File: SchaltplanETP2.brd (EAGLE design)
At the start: 110 x 60 mm, 62 parts, among them IC1 LM2674, IC2 ZXLD1350, IC3 ZXLD1350, IC4 ZXLD1350, IC5 ZXLD1350, M1 RN42_BLUETOOTH, T1 BUK98150-55A, X1 TERMINAL_BLOCK_MC000036, X2 TERMINAL_BLOCK_MC000036

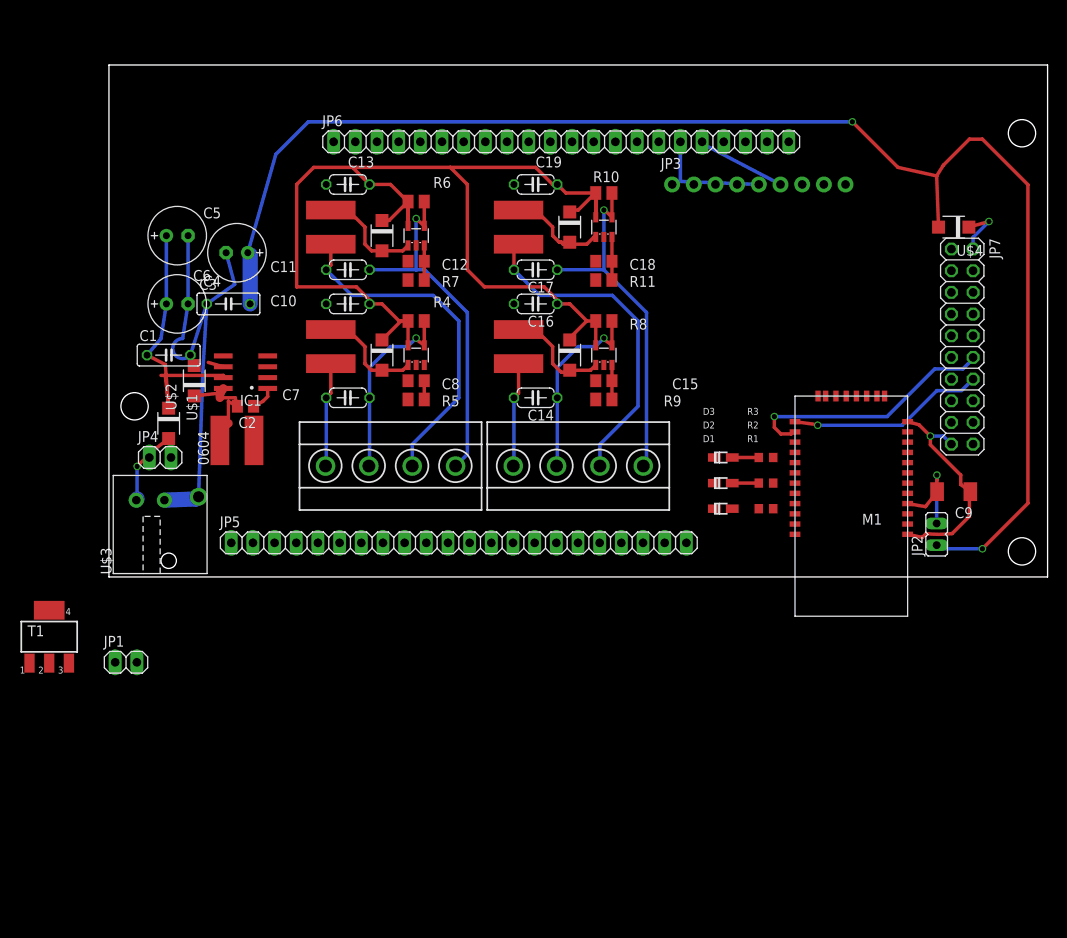
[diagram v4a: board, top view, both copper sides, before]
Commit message: added placed screw terminal and diode for motor driver
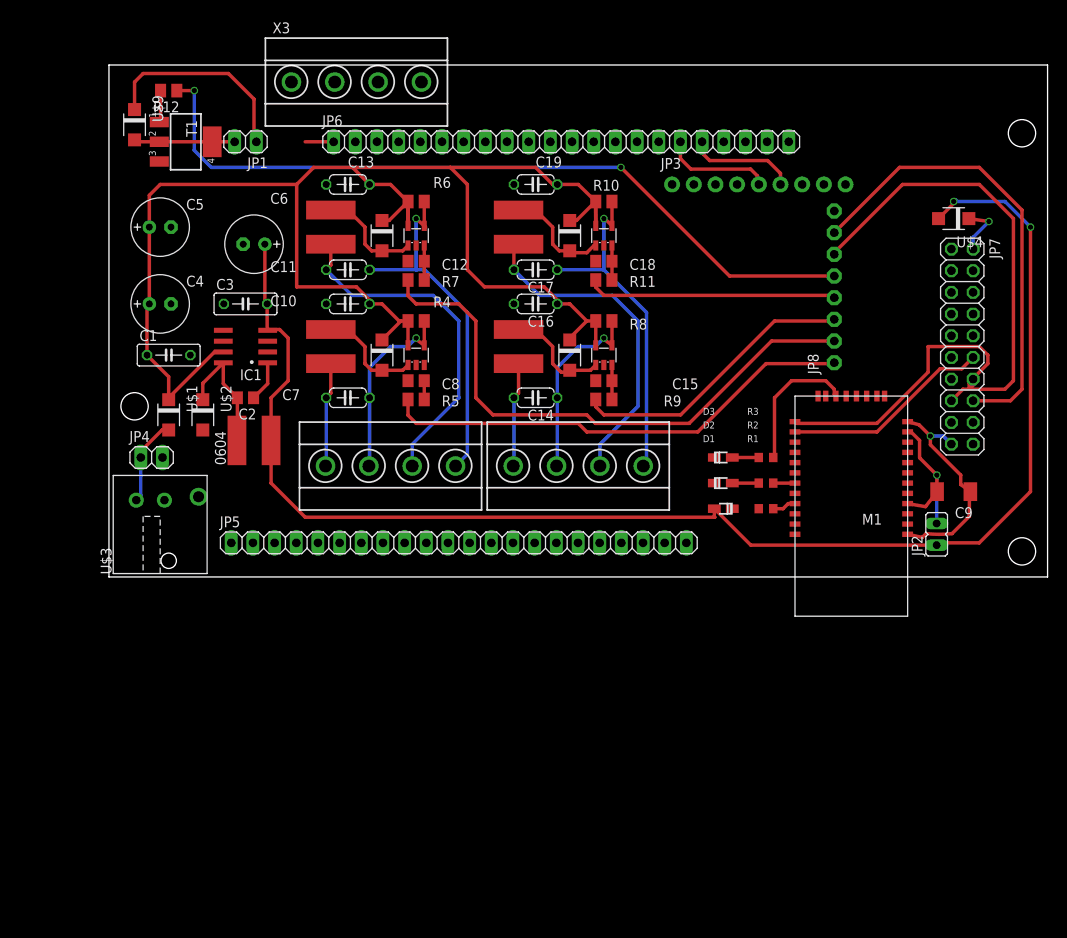
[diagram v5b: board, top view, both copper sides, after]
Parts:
- added JP8: (no value), adafruit:1X08-CLEANBIG
- added R12: 220, rcl:M0805
- added U$9: SS13L, Moodlight:SUB-SMA
- added X3: TERMINAL_BLOCK_MC000036, Moodlight:TERMINAL_BLOCK_MC000036
- moved JP1 62.6 mm to (16.0, 51.0), turned to 180 degrees
- moved T1 60.2 mm to (9.00, 51.0), turned to 270 degrees
- moved U$2 4.12 mm to (11.0, 19.0), turned to 270 degrees
- moved IC1 3.00 mm to (16.0, 27.0)
- moved C5 2.24 mm to (6.00, 41.0)
- moved C6 2.24 mm to (17.0, 39.0)
- moved 0604 2.00 mm to (17.0, 16.0)
- moved C3 2.00 mm to (16.0, 32.0)
- moved C4 2.00 mm to (6.00, 32.0)
- moved C2 1.00 mm to (16.0, 21.0)
- moved IC4 1.00 mm to (58.0, 40.0)
- moved JP4 1.00 mm to (5.00, 14.0)
- moved R10 1.00 mm to (58.0, 44.0)
- moved U$1 1.00 mm to (7.00, 19.0)
- moved U$4 1.00 mm to (99.0, 42.0)
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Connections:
- new net MCU_I2C: JP7.15, JP8.6
- new net MCU_I2C2: JP7.16, JP8.7
- new net M_PWM: JP8.5, R12.1, X3.1
- new net N$1: R12.2, T1.1
- new net N$28: JP8.8
- net 0_PWM: now also JP8.1
- net 1_PWM: now also JP8.2
- net 2_PWM: now also JP8.3
- net 3V3: now also U$9.C
- net 3_PWM: now also JP8.4
- net M-: now also U$9.A, X3.2
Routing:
- net M_PWM: track 0.00 -> 90.2 mm, vias 0 -> 2
- net 1_PWM: track 0.00 -> 67.3 mm
- net GND: track 82.8 -> 25.9 mm
- net 0_PWM: track 0.00 -> 56.0 mm
- net MCU_I2C2: track 0.00 -> 54.5 mm
- net MCU_I2C: track 0.00 -> 53.4 mm
- net 2_PWM: track 0.00 -> 33.8 mm
- net 3_PWM: track 0.00 -> 29.3 mm
- net 3V3: track 0.00 -> 24.0 mm
- net +24V: track 167.9 -> 186.2 mm
- net N$12: track 0.00 -> 16.3 mm
- net M-: track 0.00 -> 12.0 mm
- net RN42_TX: track 23.2 -> 34.9 mm, vias 1 -> 0
- net N$5: track 12.5 -> 19.2 mm
- net RN42_RX: track 30.3 -> 24.5 mm, vias 1 -> 0
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
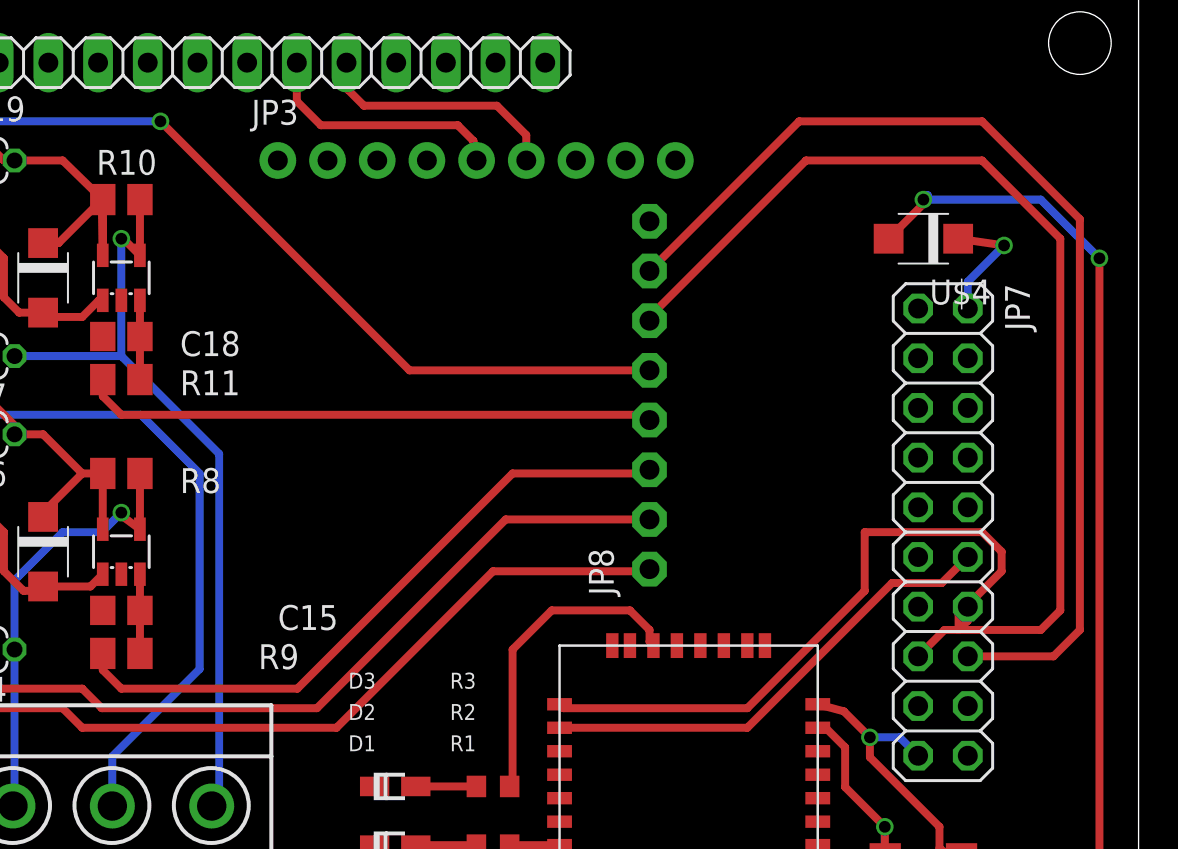
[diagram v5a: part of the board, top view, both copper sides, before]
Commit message: added PCA9685 i2c to pwm 16 channel driver
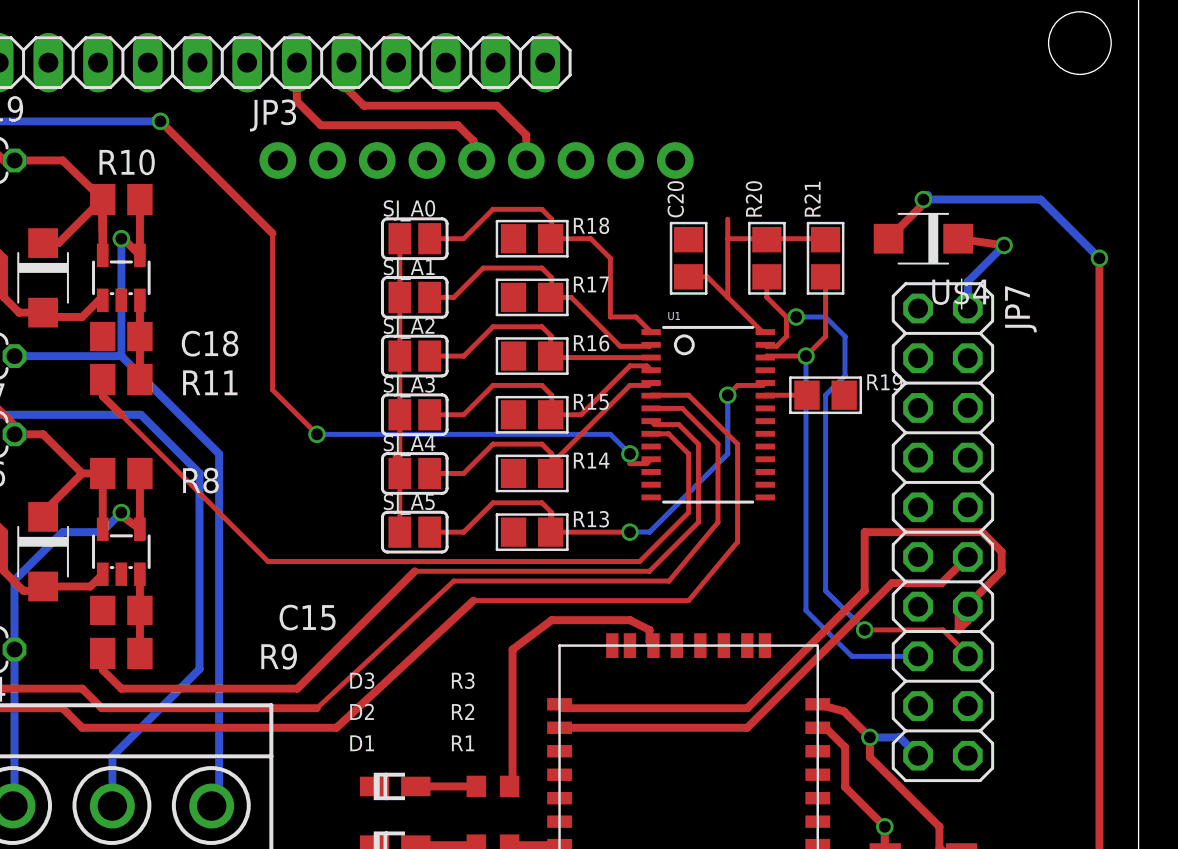
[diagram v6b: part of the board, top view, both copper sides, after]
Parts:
- removed JP8: (no value), adafruit:1X08-CLEANBIG
- added C20: 10uF, microbuilder:0805
- added R13, R14, R15, R16, R17, R18, R19, R20, R21: 10K, microbuilder:0805
- added SJ_A0, SJ_A1, SJ_A2, SJ_A3, SJ_A4, SJ_A5: (no value), microbuilder:SOLDERJUMPER_REFLOW_NOPASTE
- added U1: PCA9685, microbuilder:TSSOP28
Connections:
- removed net MCU_I2C: JP7.15, JP8.6
- removed net MCU_I2C2: JP7.16, JP8.7
- removed net N$28: JP8.8
- new net 4_PWM: U1.10
- new net A0: R18.2, SJ_A0.2, U1.1
- new net A1: R17.2, SJ_A1.2, U1.2
- new net A2: R16.2, SJ_A2.2, U1.3
- new net A3: R15.2, SJ_A3.2, U1.4
- new net A4: R14.2, SJ_A4.2, U1.5
- new net A5: R13.2, SJ_A5.2, U1.24
- new net OE: R19.1, U1.23
- new net PWM10: U1.17
- new net PWM11: U1.18
- new net PWM12: U1.19
- new net PWM13: U1.20
- new net PWM14: U1.21
- new net PWM15: U1.22
- new net PWM6: U1.12
- new net PWM7: U1.13
- new net PWM8: U1.15
- new net PWM9: U1.16
- new net SCL: JP7.15, R21.1, U1.26
- new net SDA: JP7.16, R20.1, U1.27
- new net VCC: C20.1, R20.2, R21.2, SJ_A0.1, SJ_A1.1, SJ_A2.1, SJ_A3.1, SJ_A4.1, SJ_A5.1, U1.28
- net 0_PWM: now also U1.6; no longer JP8.1
- net 1_PWM: now also U1.7; no longer JP8.2
- net 2_PWM: now also U1.8; no longer JP8.3
- net 3_PWM: now also U1.9; no longer JP8.4
- net GND: now also C20.2, R13.1, R14.1, R15.1, R16.1, R17.1, R18.1, R19.2, U1.14, U1.25
- net M_PWM: now also U1.11; no longer JP8.5
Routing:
- net MCU_I2C2: track 54.5 -> 0.00 mm
- net MCU_I2C: track 53.4 -> 0.00 mm
- net VCC: track 0.00 -> 31.3 mm
- net SDA: track 0.00 -> 30.3 mm, vias 0 -> 2
- net SCL: track 0.00 -> 26.3 mm, vias 0 -> 1
- net A5: track 0.00 -> 24.9 mm, vias 0 -> 2
- net A0: track 0.00 -> 17.0 mm
- net 0_PWM: track 56.0 -> 71.5 mm
- net A4: track 0.00 -> 15.4 mm
- net A3: track 0.00 -> 14.3 mm
- net A1: track 0.00 -> 14.3 mm
- net A2: track 0.00 -> 13.3 mm
- net 1_PWM: track 67.3 -> 78.9 mm
- net 3_PWM: track 29.3 -> 40.7 mm
- net 2_PWM: track 33.8 -> 42.1 mm
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
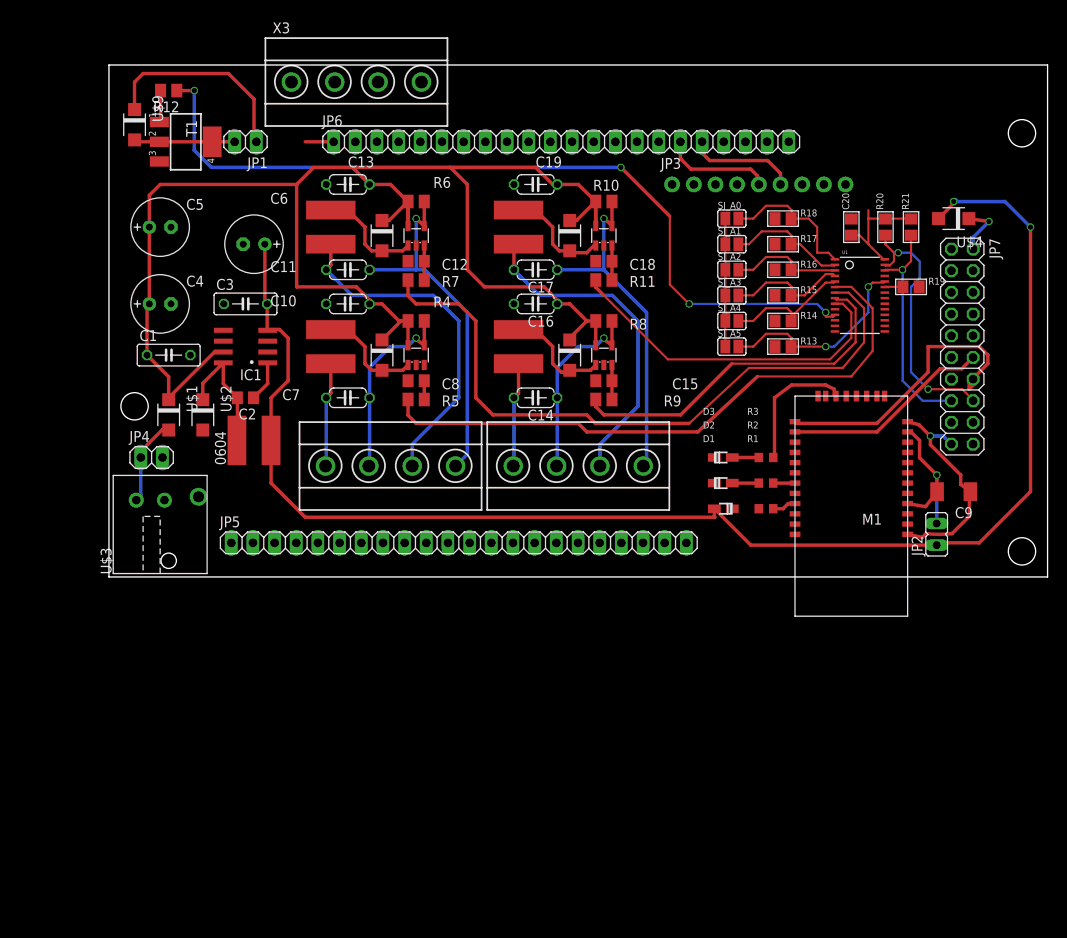
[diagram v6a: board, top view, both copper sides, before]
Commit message: rearrangement of the components
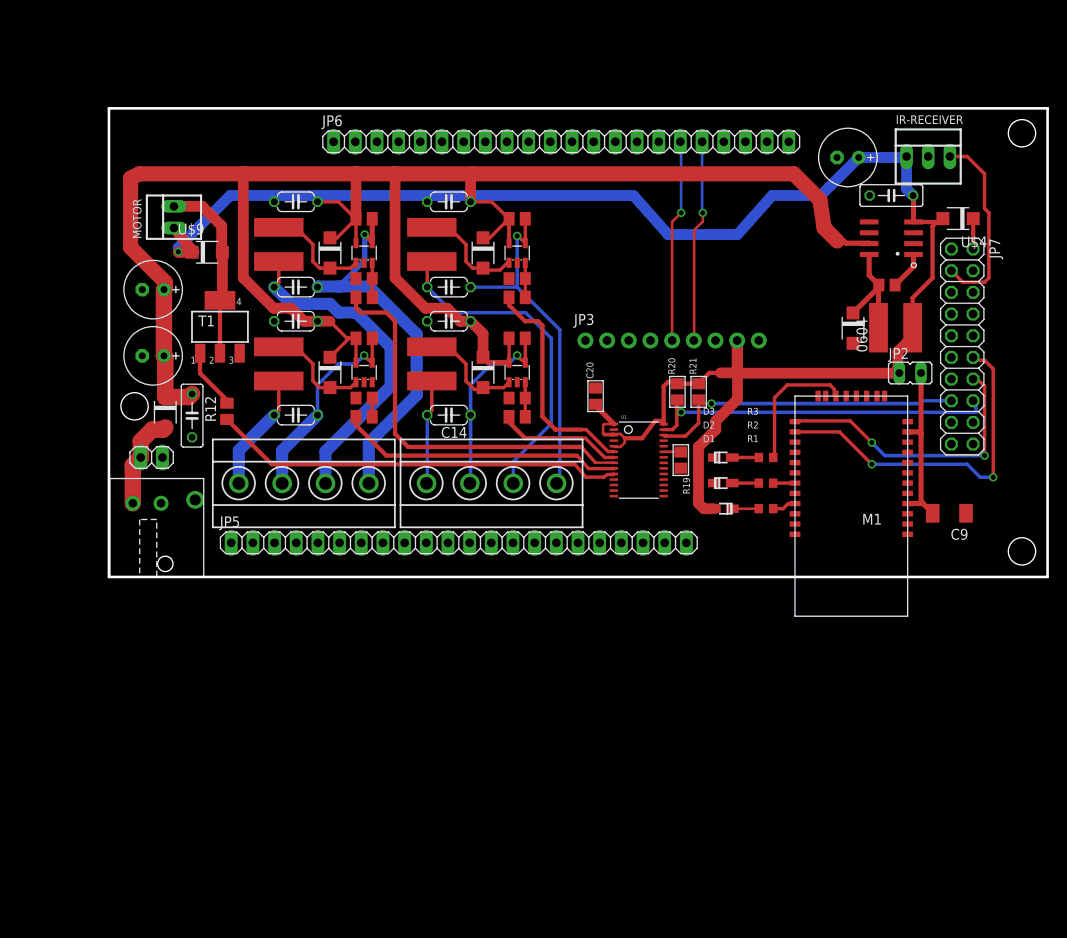
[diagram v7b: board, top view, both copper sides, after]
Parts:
- removed JP1: (no value), pinhead:1X02
- removed R13, R14, R15, R16, R17, R18: 10K, microbuilder:0805
- removed SJ_A0, SJ_A1, SJ_A2, SJ_A3, SJ_A4, SJ_A5: (no value), microbuilder:SOLDERJUMPER_REFLOW_NOPASTE
- removed X3: TERMINAL_BLOCK_MC000036, Moodlight:TERMINAL_BLOCK_MC000036
- added IR-RECEIVER: 22-23-2031, con-molex:22-23-2031
- added MOTOR: 22-23-2021, con-molex:22-23-2021
- moved U$2 76.9 mm to (87.2, 29.2)
- moved C3 76.8 mm to (91.7, 44.7)
- moved IC1 76.8 mm to (91.7, 39.7)
- moved 0604 76.3 mm to (92.2, 29.2)
- moved C2 76.3 mm to (91.2, 34.2)
- moved C6 70.3 mm to (86.6, 49.2)
- moved R12 38.2 mm to (13.8, 19.4), turned to 90 degrees
- moved C20 35.9 mm to (57.0, 21.2)
- moved R19 33.8 mm to (67.0, 13.7), turned to 270 degrees
- moved U1 32.3 mm to (62.1, 13.7)
- moved R21 31.5 mm to (69.1, 21.7)
- moved R20 31.1 mm to (66.6, 21.7)
- moved T1 22.0 mm to (13.0, 29.3), turned to 0 degrees
- moved JP3 20.9 mm to (55.8, 27.7)
- moved JP2 19.2 mm to (93.9, 23.9), turned to 270 degrees
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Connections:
- removed net +3V3: 0604.2, C3.2, C6.+, D1.A, IC1.4, JP2.1, U$4.A
- removed net 4_PWM: U1.10
- removed net 5V: JP5.1, JP6.1
- removed net A0: R18.2, SJ_A0.2, U1.1
- removed net A1: R17.2, SJ_A1.2, U1.2
- removed net A2: R16.2, SJ_A2.2, U1.3
- removed net A3: R15.2, SJ_A3.2, U1.4
- removed net A4: R14.2, SJ_A4.2, U1.5
- removed net A5: R13.2, SJ_A5.2, U1.24
- removed net VCC: C20.1, R20.2, R21.2, SJ_A0.1, SJ_A1.1, SJ_A2.1, SJ_A3.1, SJ_A4.1, SJ_A5.1, U1.28
- new net IR_IN: IR-RECEIVER.3, JP7.3
- new net PWM5: U1.11
- net 0_PWM: now also R11.1; no longer R5.1
- net 1_PWM: now also R9.1; no longer R7.1
- net 2_PWM: now also R7.1; no longer R9.1
- net 3V3: now also 0604.2, C20.1, C3.2, C6.+, D1.A, IC1.4, IR-RECEIVER.1, JP2.1, MOTOR.1, R20.2, R21.2, U$4.A, U1.1, U1.28, U1.3, U1.5; no longer JP1.1, JP5.22
- net 3_PWM: now also R5.1; no longer R11.1
- net GND: now also IR-RECEIVER.2, U1.2, U1.24, U1.4; no longer R13.1, R14.1, R15.1, R16.1, R17.1, R18.1
- net M-: now also MOTOR.2; no longer JP1.2, X3.2
- net M_PWM: now also U1.10; no longer U1.11, X3.1
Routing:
- net 3V3: track 24.0 -> 208.6 mm, vias 0 -> 1
- net +3V3: track 172.1 -> 0.00 mm, vias 2 -> 0
- net 1_PWM: track 78.9 -> 14.6 mm
- net M_PWM: track 97.3 -> 48.4 mm, vias 4 -> 0
- net 0_PWM: track 71.5 -> 26.6 mm
- net +24V: track 186.2 -> 228.1 mm
- net VCC: track 31.3 -> 0.00 mm
- net GND: track 25.9 -> 0.00 mm, vias 1 -> 0
- net A5: track 24.9 -> 0.00 mm, vias 2 -> 0
- net IR_IN: track 0.00 -> 22.5 mm
- net A0: track 17.0 -> 0.00 mm
- net RN42_RX: track 24.5 -> 41.1 mm, vias 0 -> 2
- net A4: track 15.4 -> 0.00 mm
- net A3: track 14.3 -> 0.00 mm
- net A1: track 14.3 -> 0.00 mm
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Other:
- board size 110 x 60 mm -> 110 x 54.9 mm
- board text added: "Bottom"
- board text added: "°"

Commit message: changes added polygon and some changes for version1
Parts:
- moved R19 0.51 mm to (67.0, 13.2)
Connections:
- net +24V_EINGANG renamed VIN24V
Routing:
- net GND: track 0.00 -> 26.2 mm, vias 0 -> 4
- net 3V3: track 208.6 -> 226.2 mm, vias 1 -> 2
- net +24V: track 228.1 -> 234.2 mm, vias 0 -> 1
- net N$13: track 2.20 -> 4.05 mm
- net VIN24V: vias 1 -> 0
- added copper zone on layer 1, net GND
- added copper zone on layer 16, net GND
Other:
- board text added: "24V"
- board text added: "26-3-2017"
- board text added: "3V3"
- board text added: "BOTTOM"
- board text added: "GND"
- board text added: "Marco Flueeler"
- board text added: "Noah Boateng"
- board text added: "TOP"
- board text added: "v1"
- board text added: "zhaw Moodlight"
